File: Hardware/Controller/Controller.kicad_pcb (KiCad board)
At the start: 2 copper layers, 35 x 124 mm, 52 parts, among them J1 8P8C, J2 LCD Header, J3 USB_B_Micro, J4 S88 ShiftRegister, SW1 Rotary_Encoder_Switch, SW2 SW_Push_Dual, SW3 SW_Push_Dual, SW4 SW_Push_Dual, SW5 SW_Push_Dual, SW6 SW_Push_Dual, SW7 Shift, SW8 Stop, U1 ESP32-WROOM-32, U2 TJA1051T, U3 74LS367, U4 CH340C

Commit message: Added XM1548 and worked on Hardware
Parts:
- added C11: 100n, Capacitor_SMD:C_0805_2012Metric_Pad1.15x1.40mm_HandSolder, B.Cu at (32.5, 28.5)
- added C12: 470u, Capacitor_THT:CP_Radial_D6.3mm_P2.50mm, F.Cu at (71.3, 30.9)
- added C13: 4u7, Capacitor_THT:CP_Radial_D6.3mm_P2.50mm, F.Cu at (66.0, 24.0)
- added D1: D_Schottky, Diode_SMD:D_0603_1608Metric_Pad1.05x0.95mm_HandSolder, F.Cu at (33.5, 119.0)
- added D2: D_Schottky, Diode_SMD:D_0603_1608Metric_Pad1.05x0.95mm_HandSolder, F.Cu at (40.5, 119.0)
- added D3: D_Schottky, Diode_SMD:D_0603_1608Metric_Pad1.05x0.95mm_HandSolder, B.Cu at (22.0, 107.0)
- added J5: Screw_Terminal_01x05, TerminalBlock_RND:TerminalBlock_RND_205-00015_1x05_P5.00mm_Horizontal, F.Cu at (16.5, 97.0)
- added U5: XM1584, Controller:XM1584, F.Cu at (30.5, 106.5)
- C1, C10, C2, C3, C4, C5, C6, C7, C8, C9, R1, R10, R11, R12, R13, R14, R15, R16, R17, R18, R19, R2, R20, R3, R4, R5, R6, R7, R9: moved to F.Cu
- SW1, SW2, SW3, SW4, SW5, SW6, SW7, SW8: moved to B.Cu
- moved R6 56.3 mm to (19.0, 76.5)
- moved C3 54.8 mm to (22.5, 75.5), turned to 270 degrees
- moved C4 49.7 mm to (18.0, 86.0), turned to 90 degrees
- moved R10 48.5 mm to (30.1, 76.2)
- moved C6 47.7 mm to (29.2, 85.8), turned to 90 degrees
- moved R12 45.1 mm to (32.9, 84.8), turned to 180 degrees
- moved R11 44.1 mm to (35.8, 81.9), turned to 90 degrees
- moved C9 43.3 mm to (41.5, 60.5), turned to 90 degrees
- moved C5 42.8 mm to (33.8, 75.2), turned to 270 degrees
- moved R18 39.6 mm to (45.2, 59.5), turned to 180 degrees
- moved R15 38.1 mm to (45.8, 81.9), turned to 90 degrees
- moved R17 36.9 mm to (43.8, 56.8), turned to 90 degrees
- moved R13 36.7 mm to (41.2, 79.2), turned to 270 degrees
- moved R16 36.7 mm to (43.0, 84.8), turned to 180 degrees
- moved R14 34.9 mm to (40.1, 76.5)
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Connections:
- net Net-(J1-Pad1) renamed /CANH
- net Net-(J1-Pad2) renamed /CANL
- J1 pad 3: Net-(J1-Pad3) -> Net-(D1-Pad2)
- J1 pad 4: Net-(J1-Pad4) -> Net-(D1-Pad2)
- U1 pad 30: Net-(U1-Pad30) -> Net-(C1-Pad2)
- U1 pad 33: Net-(U1-Pad33) -> Net-(C2-Pad2)
- U1 pad 36: Net-(U1-Pad36) -> Net-(C10-Pad2)
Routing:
- net GND: track 0.00 -> 295.0 mm, vias 0 -> 7
- net VCC: track 66.6 -> 173.8 mm, vias 3 -> 2
- net /CANL: track 106.6 -> 15.4 mm
- net /CANH: track 100.9 -> 13.1 mm
- net Net-(D1-Pad1): track 0.00 -> 25.4 mm, vias 0 -> 1
- net Net-(D1-Pad2): track 0.00 -> 8.67 mm
- net Net-(R10-Pad1): track 0.00 -> 6.85 mm
- net Net-(R5-Pad1): track 0.00 -> 6.66 mm
- net Net-(R17-Pad1): track 0.00 -> 6.66 mm
- net Net-(R13-Pad1): track 0.00 -> 6.60 mm
- net Net-(D3-Pad2): track 0.00 -> 4.62 mm
- net Net-(R15-Pad1): track 0.00 -> 4.05 mm
- net Net-(R7-Pad1): track 0.00 -> 4.00 mm
- net Net-(R11-Pad1): track 0.00 -> 4.00 mm
- net Net-(D2-Pad2): track 0.00 -> 3.76 mm
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
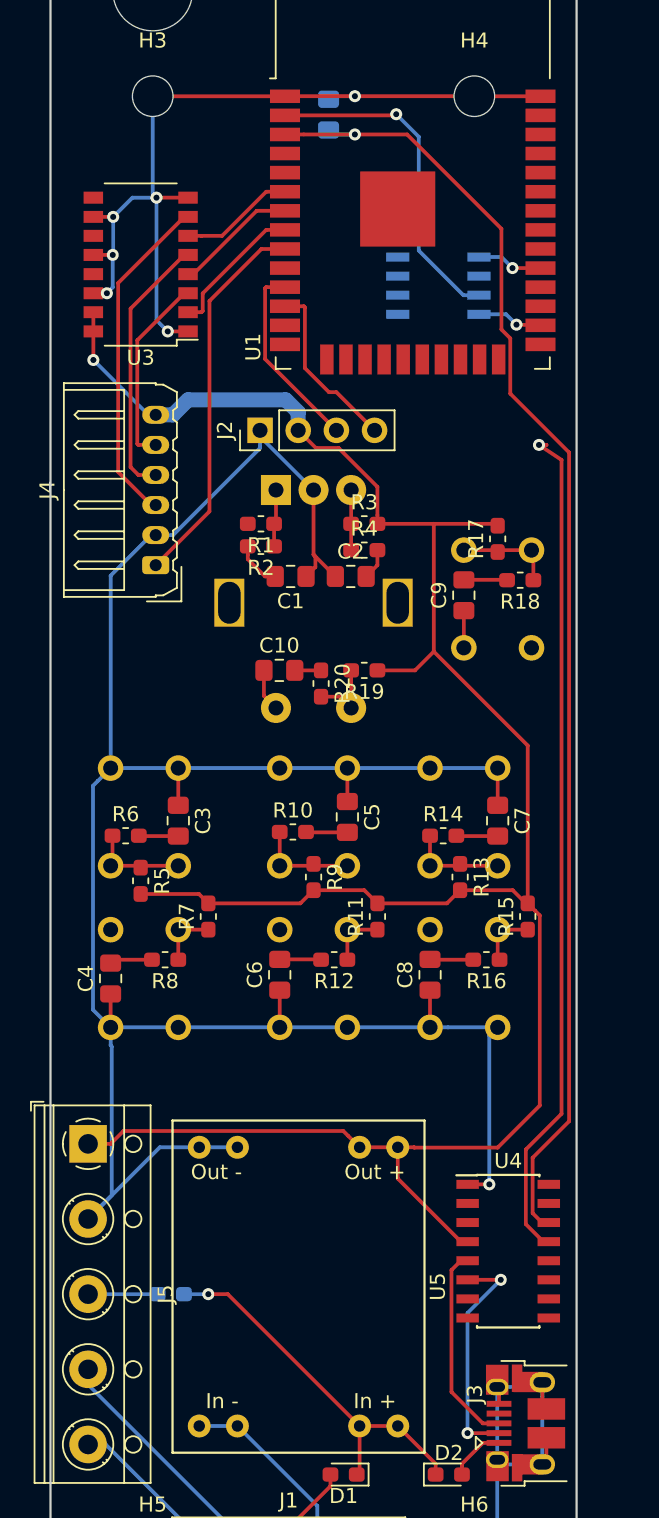
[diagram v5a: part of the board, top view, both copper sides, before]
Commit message: Switched to all-SMD Buttons
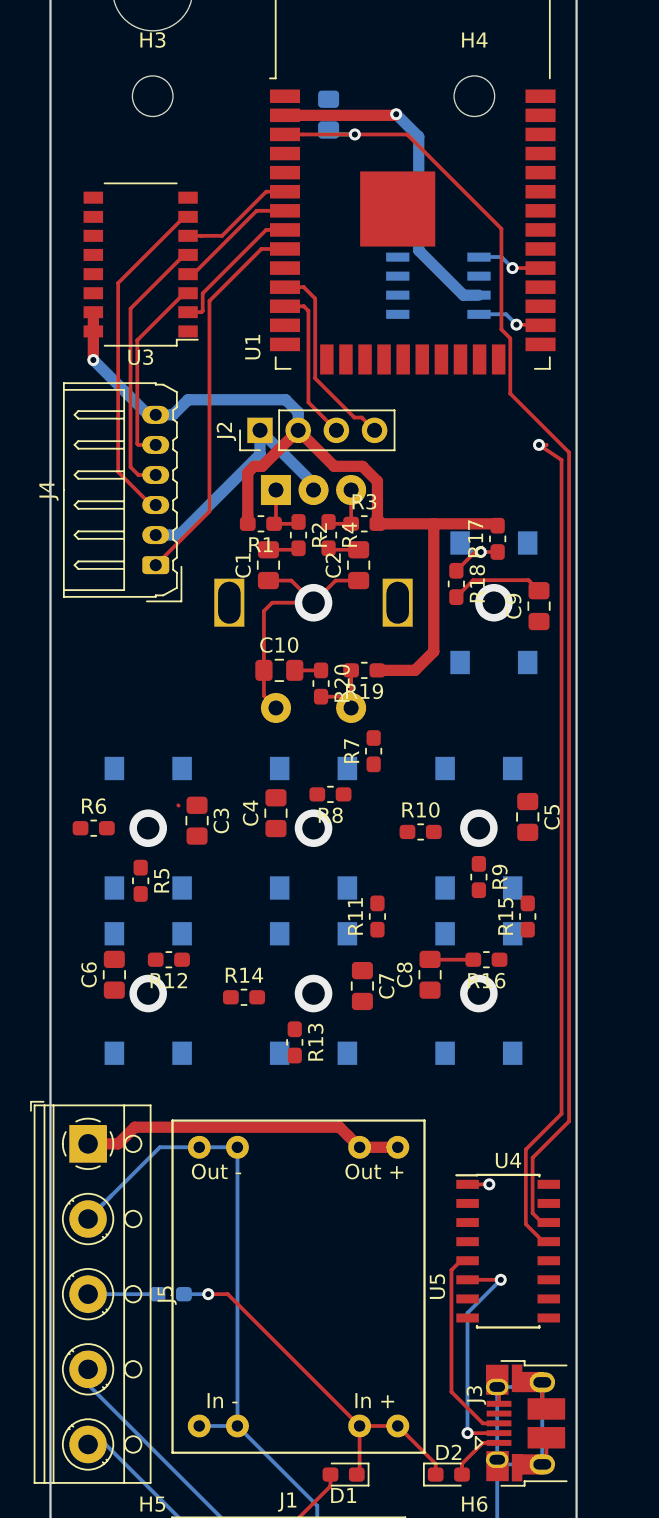
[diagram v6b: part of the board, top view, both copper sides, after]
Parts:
- SW2: value SW_Push_Dual -> SW_F0; footprint Button_Switch_THT:SW_TH_Tactile_Omron_B3F-10xx -> Button_Switch_SMD:SW_SPST_B3S-1000
- SW3: value SW_Push_Dual -> SW_F1; footprint Button_Switch_THT:SW_TH_Tactile_Omron_B3F-10xx -> Button_Switch_SMD:SW_SPST_B3S-1000
- SW4: value SW_Push_Dual -> SW_F2; footprint Button_Switch_THT:SW_TH_Tactile_Omron_B3F-10xx -> Button_Switch_SMD:SW_SPST_B3S-1000
- SW5: value SW_Push_Dual -> SW_F3; footprint Button_Switch_THT:SW_TH_Tactile_Omron_B3F-10xx -> Button_Switch_SMD:SW_SPST_B3S-1000
- SW6: value SW_Push_Dual -> SW_F4; footprint Button_Switch_THT:SW_TH_Tactile_Omron_B3F-10xx -> Button_Switch_SMD:SW_SPST_B3S-1000
- SW7, SW8: footprint Button_Switch_THT:SW_TH_Tactile_Omron_B3F-10xx -> Button_Switch_SMD:SW_SPST_B3S-1000
- moved R14 17.1 mm to (26.9, 87.2)
- moved C4 15.6 mm to (29.0, 75.0)
- moved R13 15.6 mm to (30.2, 90.2)
- moved R7 15.6 mm to (35.5, 70.9)
- moved R8 15.6 mm to (32.6, 73.8)
- moved SW3 15.1 mm to (31.5, 76.0), turned to 90 degrees
- moved SW6 14.9 mm to (31.5, 87.0)
- moved C7 14.2 mm to (34.8, 86.5)
- moved C5 12.0 mm to (45.8, 75.2)
- moved C6 11.0 mm to (18.2, 85.8)
- moved R12 11.0 mm to (21.9, 84.8)
- moved R9 11.0 mm to (42.5, 79.2)
- moved SW5 9.73 mm to (20.5, 87.0), turned to 90 degrees
- moved SW4 9.10 mm to (42.5, 76.0)
- moved R10 8.50 mm to (38.6, 76.2)
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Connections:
- net Net-(C1-Pad2) renamed /Encoder_A
- net Net-(C10-Pad2) renamed /Encoder_Button
- net Net-(C11-Pad1) renamed /EN
- net Net-(C2-Pad2) renamed /EncoderB
- net Net-(C3-Pad2) renamed /F0
- net Net-(C4-Pad2) renamed /F1
- net Net-(C5-Pad2) renamed /F2
- net Net-(C6-Pad2) renamed /F3
- net Net-(C7-Pad2) renamed /F4
- net Net-(C8-Pad2) renamed /Shift
- net Net-(C9-Pad2) renamed /Stop
- net Net-(U1-Pad25) renamed /GPIO0
- net Net-(U1-Pad34) renamed /RX0
- net Net-(U1-Pad35) renamed /TX0
- J1 pad 7: Net-(J1-Pad7) -> (no net)
- J1 pad 8: Net-(J1-Pad8) -> (no net)
- J3 pad 4: Net-(J3-Pad4) -> (no net)
- U1 pad 10: Net-(U1-Pad10) -> (no net)
- U1 pad 11: /I2C_SCL -> /I2C_SDA
- U1 pad 12: /I2C_SDA -> /I2C_SCL
- U1 pad 17: Net-(U1-Pad17) -> (no net)
- U1 pad 18: Net-(U1-Pad18) -> (no net)
- U1 pad 19: Net-(U1-Pad19) -> (no net)
- U1 pad 20: Net-(U1-Pad20) -> (no net)
- U1 pad 21: Net-(U1-Pad21) -> (no net)
- U1 pad 22: Net-(U1-Pad22) -> (no net)
- U1 pad 24: Net-(U1-Pad24) -> (no net)
- U1 pad 32: Net-(U1-Pad32) -> (no net)
- U1 pad 37: Net-(U1-Pad37) -> (no net)
- U1 pad 4: Net-(U1-Pad4) -> (no net)
- U1 pad 5: Net-(U1-Pad5) -> (no net)
- U2 pad 5: Net-(U2-Pad5) -> (no net)
- U2 pad 8: Net-(U2-Pad8) -> (no net)
- U3 pad 11: Net-(U3-Pad11) -> (no net)
- U3 pad 13: Net-(U3-Pad13) -> (no net)
- U3 pad 9: Net-(U3-Pad9) -> (no net)
- U4 pad 10: Net-(U4-Pad10) -> (no net)
- U4 pad 11: Net-(U4-Pad11) -> (no net)
- U4 pad 12: Net-(U4-Pad12) -> (no net)
- U4 pad 15: Net-(U4-Pad15) -> (no net)
- U4 pad 7: Net-(U4-Pad7) -> (no net)
- U4 pad 8: Net-(U4-Pad8) -> (no net)
- U4 pad 9: Net-(U4-Pad9) -> (no net)
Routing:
- net GND: track 295.0 -> 135.9 mm, vias 7 -> 9
- net VCC: track 173.8 -> 102.4 mm
- net Net-(R10-Pad1): track 6.85 -> 0.35 mm
- net Net-(R5-Pad1): track 6.66 -> 0.35 mm
- net Net-(R13-Pad1): track 6.60 -> 0.35 mm
- net Net-(R15-Pad1): track 4.05 -> 0.00 mm
- net Net-(R7-Pad1): track 4.00 -> 0.00 mm
- net Net-(R11-Pad1): track 4.00 -> 0.00 mm
- net /Stop: track 2.89 -> 6.26 mm
- net /F4: track 2.76 -> 0.00 mm
- net /F2: track 2.76 -> 0.00 mm
- net /F3: track 2.76 -> 0.04 mm
- net /F0: track 2.64 -> 0.00 mm
- net /F1: track 2.84 -> 0.32 mm
- net /I2C_SCL: track 12.8 -> 10.4 mm
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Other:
- net class Power added: clearance 0.2, trace_width 0.75, via_dia 0.8, via_drill 0.4

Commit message: Finished PCB
* Reordered some pins to make the PCB layout easier
* Added connector descriptions
* Adjusted Silkscreen Items
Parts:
- C12: footprint Capacitor_THT:CP_Radial_D6.3mm_P2.50mm -> Capacitor_SMD:CP_Elec_6.3x7.7
- C13: footprint Capacitor_THT:CP_Radial_D6.3mm_P2.50mm -> Capacitor_Tantalum_SMD:CP_EIA-3216-18_Kemet-A_Pad1.58x1.35mm_HandSolder
- H3, H4, H5, H6: footprint MountingHole:MountingHole_2.7mm_M2.5 -> MountingHole:MountingHole_2.7mm_M2.5_Pad_Via
- J4: value S88 ShiftRegister -> S88
- U3, U4: moved to B.Cu
- moved U4 71.5 mm to (35.0, 33.2), turned to 180 degrees
- moved C12 50.8 mm to (20.6, 34.5)
- moved C13 40.2 mm to (26.0, 28.4)
- moved R11 16.0 mm to (19.8, 82.4)
- moved R7 10.3 mm to (32.2, 80.6), turned to 270 degrees
- moved R6 8.09 mm to (24.9, 77.1), turned to 90 degrees
- moved R13 7.89 mm to (30.8, 82.4), turned to 90 degrees
- moved R14 7.67 mm to (34.1, 84.8), turned to 180 degrees
- moved R10 6.08 mm to (44.7, 76.1), turned to 90 degrees
- moved C7 6.05 mm to (28.8, 85.8), turned to 90 degrees
- moved C9 5.94 mm to (41.0, 63.5)
- moved U2 5.06 mm to (35.0, 41.5)
- moved C4 5.04 mm to (34.0, 75.2), turned to 270 degrees
- moved R8 4.62 mm to (35.8, 77.1), turned to 90 degrees
- moved C5 4.30 mm to (42.5, 72.4)
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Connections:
- net Net-(D1-Pad1) renamed /VinCommon
- net Net-(D1-Pad2) renamed /VinCAN
- net Net-(D2-Pad2) renamed /VinUsb
- net Net-(D3-Pad2) renamed /VinTerminal
- net Net-(J3-Pad2) renamed /USB-
- net Net-(J3-Pad3) renamed /USB+
- net Net-(J4-Pad4) renamed /S88_PS
- net Net-(U1-Pad26) renamed /CANRx
- net Net-(U1-Pad29) renamed /CANTx
- J4 pad 3: Net-(J4-Pad3) -> /S88_CLOCK
- J4 pad 5: Net-(J4-Pad5) -> /S88_RESET
- U1 pad 13: /F2 -> /F3
- U1 pad 23: /F3 -> /F2
- U1 pad 27: /F4 -> /Shift
- U1 pad 28: /Shift -> /F4
- U1 pad 30: /Encoder_A -> /Stop
- U1 pad 31: /Stop -> /Encoder_A
- U1 pad 6: /S88_CLOCK_UC -> /S88_DATA
- U1 pad 7: /S88_PS_UC -> /S88_CLOCK_UC
- U1 pad 8: /S88_RESET_UC -> /S88_PS_UC
- U1 pad 9: /S88_DATA -> /S88_RESET_UC
- U3 pad 2: /S88_RESET_UC -> /S88_CLOCK_UC
- U3 pad 3: Net-(J4-Pad5) -> /S88_CLOCK
- U3 pad 6: /S88_CLOCK_UC -> /S88_RESET_UC
- U3 pad 7: Net-(J4-Pad3) -> /S88_RESET
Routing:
- net GND: track 135.9 -> 514.8 mm, vias 9 -> 20
- net VCC: track 102.4 -> 252.3 mm, vias 2 -> 6
- net /CANH: track 13.1 -> 102.4 mm, vias 0 -> 1
- net /CANL: track 15.4 -> 96.8 mm, vias 0 -> 2
- net /EN: track 88.6 -> 7.35 mm
- net /USB+: track 13.5 -> 92.6 mm, vias 0 -> 1
- net /USB-: track 15.4 -> 92.0 mm, vias 2 -> 1
- net /F4: track 0.00 -> 61.6 mm, vias 0 -> 3
- net /Encoder_Button: track 1.75 -> 56.7 mm
- net /F3: track 0.04 -> 53.3 mm, vias 0 -> 1
- net /Shift: track 2.89 -> 55.1 mm, vias 0 -> 2
- net /F1: track 0.32 -> 49.6 mm, vias 0 -> 2
- net /F0: track 0.00 -> 46.8 mm
- net /EncoderB: track 2.04 -> 40.8 mm, vias 0 -> 2
- net /Encoder_A: track 2.04 -> 38.2 mm, vias 0 -> 2
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- added copper zone on B.Cu, net GND
- added copper zone on F.Cu, net GND
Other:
- board text added: "GND VCC SCL SDA"
- board text added: "RR32Can Controller V1.0"
- board text added: "VCC GND Vin CANL CANH"
- board text added: "VCC RES PS CLK GND DATA"

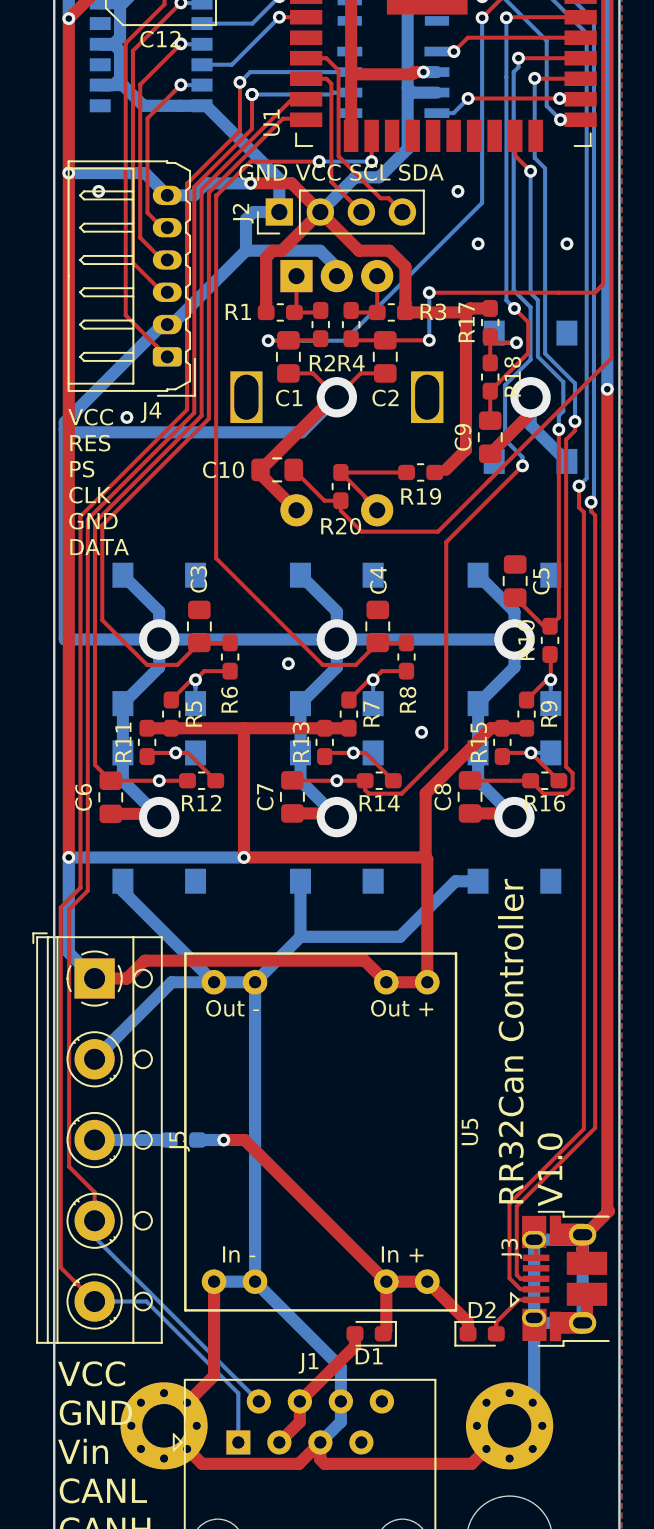
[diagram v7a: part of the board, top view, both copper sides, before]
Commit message: Updated USB Port
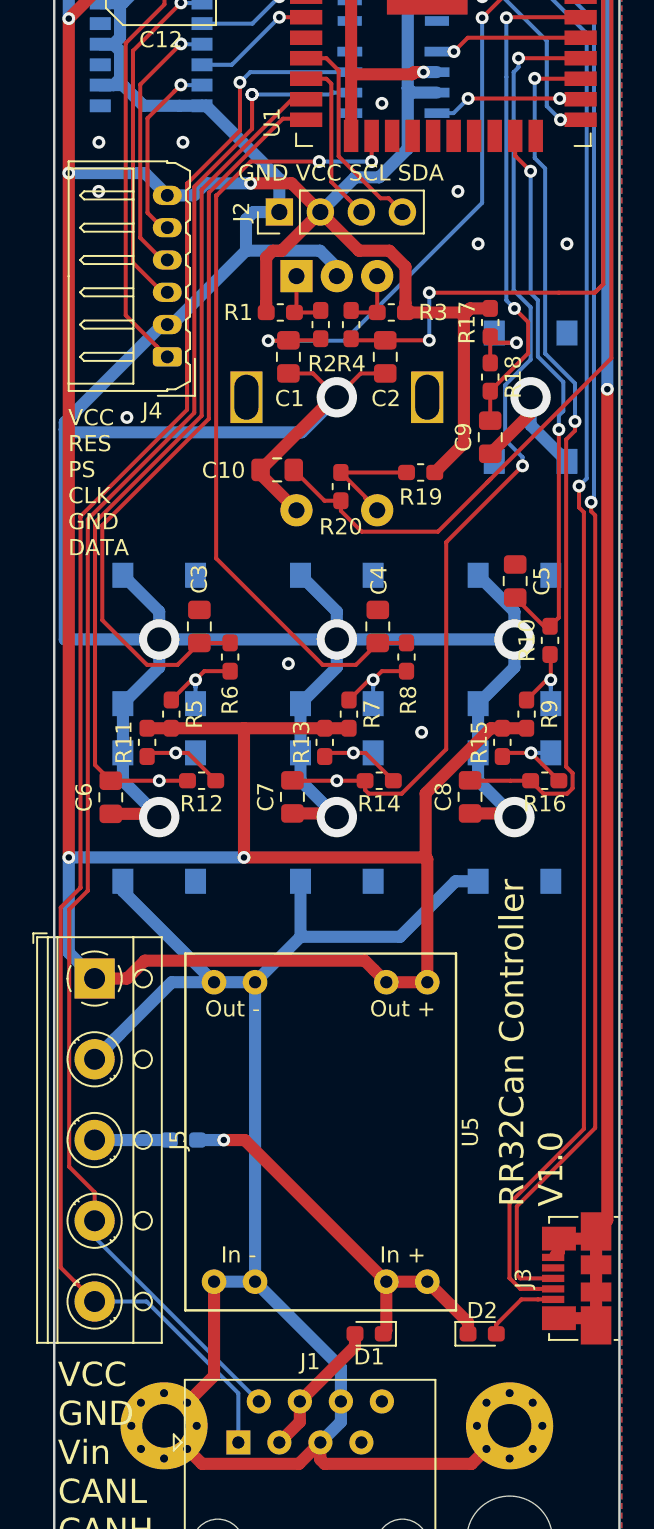
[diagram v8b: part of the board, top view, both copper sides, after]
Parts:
- J3: footprint Connector_USB:USB_Micro-B_Amphenol_10103594-0001LF_Horizontal -> Connector_USB:USB_Micro-B_Molex_47346-0001
- moved J3 0.75 mm to (46.4, 115.6)
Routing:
- net GND: track 514.8 -> 497.1 mm, vias 20 -> 23
- net /USB-: track 92.0 -> 93.1 mm
- net /USB+: track 92.6 -> 93.6 mm
- net /VinUsb: track 3.76 -> 4.74 mm
